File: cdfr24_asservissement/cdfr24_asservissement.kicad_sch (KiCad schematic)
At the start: 58 parts, among them J1 Connecteur batterie, J10 Free Connecteur, J11 Conn_01x02, J12 Conn_01x02, J13 Connecteur Odométrie, J2 Conn_01x03, J3 Conn_01x05, J4 Connecteur Programmation, J5 Conn_01x03, J6 Connecteur Odométrie, J7 Conn_01x03, Q13 Q_NMOS_GDS, U1 LM317_SOT-223, U3 STM32F401RCTx, U4 LMR16020PDDA, U4 LSM6DSL, Y1 Crystal_GND24

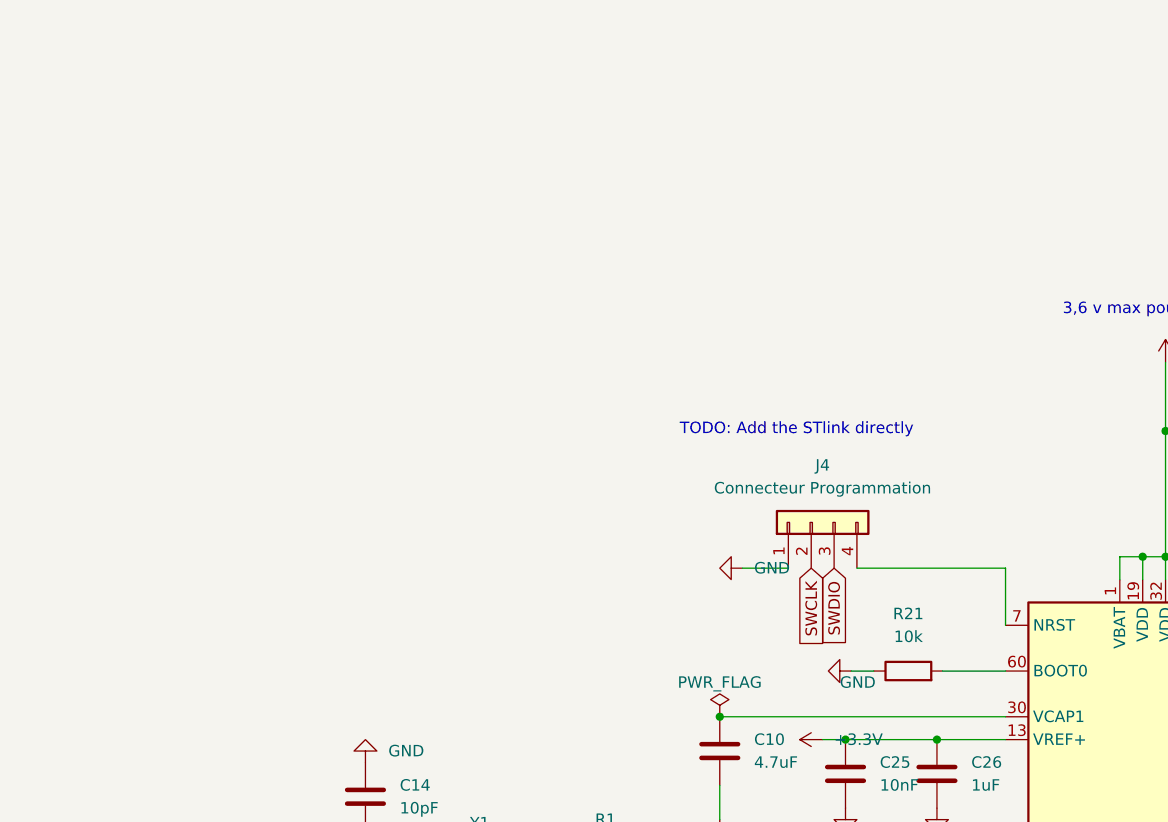
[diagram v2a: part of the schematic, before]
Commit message: new connecteur stlink
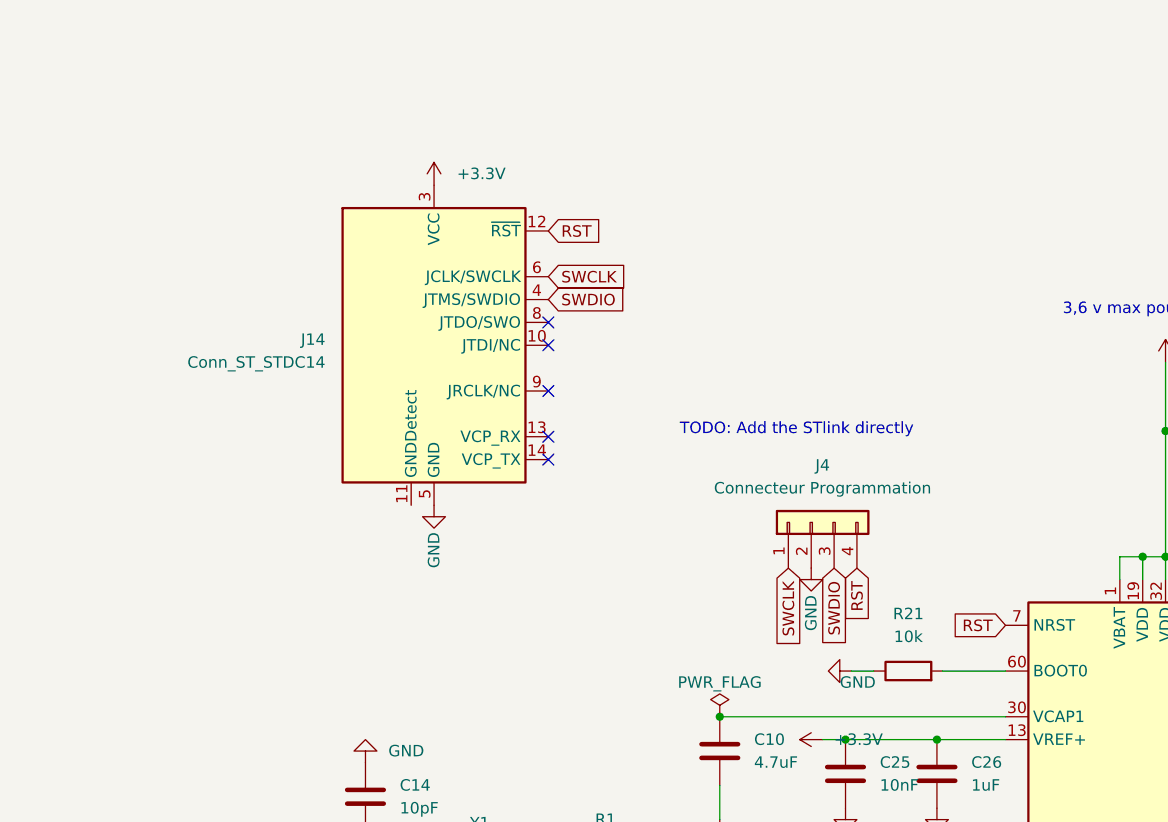
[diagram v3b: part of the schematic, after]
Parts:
- added J14: Conn_ST_STDC14, FTSH-107-01-L-DV-K-A:SAMTEC_FTSH-107-01-L-DV-K-A, symbol Connector:Conn_ST_STDC14
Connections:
- net +3.3V: now also J14.3 (VCC)
- net GND: now also J4.2 (Pin_2), J14.5 (GND), J14.7 (GND); no longer J4.1 (Pin_1)
- net SWCLK: now also J4.1 (Pin_1), J14.6 (JCLK/SWCLK); no longer J4.2 (Pin_2)
- net SWDIO: now also J14.4 (JTMS/SWDIO)
- net RST: now reaches J4.4 (Pin_4), U3.7 (NRST)
- net RST: now also J14.12 (~{RST})
- no-connect marks 15 -> 20
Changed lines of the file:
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@@
   (junction (at 145.415 236.22) (diameter 0) (color 0 0 0 0)
   )
+  (no_connect (at 79.375 225.425))
+  (no_connect (at 79.375 212.725))
   (no_connect (at 163.195 320.04))
   (no_connect (at 130.175 307.34))
@@
   (no_connect (at 163.195 289.56))
   (no_connect (at 130.175 309.88))
+  (no_connect (at 79.375 210.185))
   (no_connect (at 83.185 53.975))
   (no_connect (at 163.195 314.96))
@@
   (no_connect (at 163.195 269.24))
   (no_connect (at 130.175 279.4))
+  (no_connect (at 79.375 222.885))
   (no_connect (at 163.195 254))
+  (no_connect (at 79.375 217.805))
   (no_connect (at 163.195 264.16))
   (no_connect (at 163.195 307.34))
@@
     (stroke (width 0) (type default))
   )
-  (wire (pts (xy 113.665 237.49) (xy 130.175 237.49))
-    (stroke (width 0) (type default))
-  )
   (wire (pts (xy 145.415 236.22) (xy 147.955 236.22))
     (stroke (width 0) (type default))
@@
     (stroke (width 0) (type default))
   )
-  (wire (pts (xy 100.965 237.49) (xy 106.045 237.49))
-    (stroke (width 0) (type default))
-  )
   (wire (pts (xy 36.195 40.005) (xy 36.195 59.055))
     (stroke (width 0) (type default))
@@
     (stroke (width 0) (type default))
   )
-  (wire (pts (xy 130.175 237.49) (xy 130.175 243.84))
-    (stroke (width 0) (type default))
-  )
   (wire (pts (xy 222.885 280.67) (xy 229.235 280.67))
     (stroke (width 0) (type default))
@@
     )
   )
+  (global_label "SWDIO" (shape input) (at 79.375 207.645 0) (fields_autoplaced)
+    (effects (font (size 1.27 1.27)) (justify left))
+    (property "Intersheetrefs" "${INTERSHEET_REFS}" (at 88.147 207.645 0)
+      (effects (font (size 1.27 1.27)) (justify left) hide)
+    )
+  )
   (global_label "Free5" (shape input) (at 103.505 288.29 0) (fields_autoplaced)
     (effects (font (size 1.27 1.27)) (justify left))
@@
     )
   )
+  (global_label "RST" (shape input) (at 113.665 237.49 270) (fields_autoplaced)
+    (effects (font (size 1.27 1.27)) (justify right))
+    (property "Intersheetrefs" "${INTERSHEET_REFS}" (at 113.665 243.8429 90)
+      (effects (font (size 1.27 1.27)) (justify right) hide)
+    )
+  )
   (global_label "SWCLK" (shape input) (at 163.195 279.4 0) (fields_autoplaced)
     (effects (font (size 1.27 1.27)) (justify left))
@@
     )
   )
+  (global_label "SWCLK" (shape input) (at 79.375 205.105 0) (fields_autoplaced)
+    (effects (font (size 1.27 1.27)) (justify left))
+    (property "Intersheetrefs" "${INTERSHEET_REFS}" (at 88.5098 205.105 0)
+      (effects (font (size 1.27 1.27)) (justify left) hide)
+    )
+  )
   (global_label "Free6" (shape input) (at 103.505 290.83 0) (fields_autoplaced)
     (effects (font (size 1.27 1.27)) (justify left))
@@
     )
   )
+  (global_label "RST" (shape input) (at 79.375 200.025 0) (fields_autoplaced)
+    (effects (font (size 1.27 1.27)) (justify left))
+    (property "Intersheetrefs" "${INTERSHEET_REFS}" (at 85.7279 200.025 0)
+      (effects (font (size 1.27 1.27)) (justify left) hide)
+    )
+  )
   (global_label "Free7" (shape input) (at 103.505 293.37 0) (fields_autoplaced)
     (effects (font (size 1.27 1.27)) (justify left))
@@
     )
   )
-  (global_label "SWCLK" (shape input) (at 108.585 237.49 270) (fields_autoplaced)
+  (global_label "SWCLK" (shape input) (at 106.045 237.49 270) (fields_autoplaced)
     (effects (font (size 1.27 1.27)) (justify right))
-    (property "Intersheetrefs" "${INTERSHEET_REFS}" (at 108.6644 246.1321 90)
+    (property "Intersheetrefs" "${INTERSHEET_REFS}" (at 106.1244 246.1321 90)
       (effects (font (size 1.27 1.27)) (justify right) hide)
     )
@@
     )
   )
+  (global_label "RST" (shape input) (at 130.175 243.84 180) (fields_autoplaced)
+    (effects (font (size 1.27 1.27)) (justify right))
+    (property "Intersheetrefs" "${INTERSHEET_REFS}" (at 123.8221 243.84 0)
+      (effects (font (size 1.27 1.27)) (justify right) hide)
+    )
+  )
   (symbol (lib_id "power:+3.3V") (at 147.955 214.63 0) (unit 1)
     (in_bom yes) (on_board yes) (dnp no) (fields_autoplaced)
@@
     )
   )
-  (symbol (lib_id "power:GND") (at 100.965 237.49 270) (unit 1)
-    (in_bom yes) (on_board yes) (dnp no) (fields_autoplaced)
-    (property "Reference" "#PWR026" (at 94.615 237.49 0)
+  (symbol (lib_id "power:GND") (at 108.585 237.49 0) (unit 1)
+    (in_bom yes) (on_board yes) (dnp no)
+    (property "Reference" "#PWR026" (at 108.585 243.84 0)
       (effects (font (size 1.27 1.27)) hide)
     )
-    (property "Value" "GND" (at 102.235 237.4899 90)
+    (property "Value" "GND" (at 108.585 244.475 90)
       (effects (font (size 1.27 1.27)) (justify left))
     )
-    (property "Footprint" "" (at 100.965 237.49 0)
+    (property "Footprint" "" (at 108.585 237.49 0)
       (effects (font (size 1.27 1.27)) hide)
     )
-    (property "Datasheet" "" (at 100.965 237.49 0)
+    (property "Datasheet" "" (at 108.585 237.49 0)
       (effects (font (size 1.27 1.27)) hide)
     )
@@
     )
   )
+  (symbol (lib_id "power:+3.3V") (at 66.675 194.945 0) (unit 1)
+    (in_bom yes) (on_board yes) (dnp no) (fields_autoplaced)
+    (property "Reference" "#PWR025" (at 66.675 198.755 0)
+      (effects (font (size 1.27 1.27)) hide)
+    )
+    (property "Value" "+3.3V" (at 69.215 193.6749 0)
+      (effects (font (size 1.27 1.27)) (justify left))
+    )
+    (property "Footprint" "" (at 66.675 194.945 0)
+      (effects (font (size 1.27 1.27)) hide)
+    )
+    (property "Datasheet" "" (at 66.675 194.945 0)
+      (effects (font (size 1.27 1.27)) hide)
+    )
+    (pin "1")
+    (instances
+      (project "Asservissement_CDFR_2023"
+        (path "/aba37299-4f54-471d-ab35-d760532fd54c"
+          (reference "#PWR025") (unit 1)
+        )
+      )
+      (project "cdfr24_asservissement"
+        (path "/c6b82269-16f5-49e6-8b51-4d12a40a3077"
+          (reference "#PWR043") (unit 1)
+        )
+      )
+    )
+  )
   (symbol (lib_id "Device:Crystal_GND24") (at 59.055 270.51 90) (unit 1)
     (in_bom yes) (on_board yes) (dnp no) (fields_autoplaced)
@@
     )
   )
+  (symbol (lib_id "Connector:Conn_ST_STDC14") (at 66.675 212.725 0) (unit 1)
+    (in_bom yes) (on_board yes) (dnp no) (fields_autoplaced)
+    (property "Reference" "J14" (at 54.61 212.09 0)
+      (effects (font (size 1.27 1.27)) (justify right))
+    )
+    (property "Value" "Conn_ST_STDC14" (at 54.61 214.63 0)
+      (effects (font (size 1.27 1.27)) (justify right))
+    )
+    (property "Footprint" "FTSH-107-01-L-DV-K-A:SAMTEC_FTSH-107-01-L-DV-K-A" (at 66.675 212.725 0)
+      (effects (font (size 1.27 1.27)) hide)
+    )
+    (property "Datasheet" "https://www.st.com/content/ccc/resource/technical/document/user_manual/group1/99/49/91/b6/b2/3a/46/e5/DM00526767/files/DM00526767.pdf/jcr:content/translations/en.DM00526767.pdf" (at 57.785 244.475 90)
+      (effects (font (size 1.27 1.27)) hide)
+    )
+    (pin "1")
+    (pin "10")
+    (pin "11")
+    (pin "12")
+    (pin "13")
+    (pin "14")
+    (pin "2")
+    (pin "3")
+    (pin "4")
+    (pin "5")
+    (pin "6")
+    (pin "7")
+    (pin "8")
+    (pin "9")
+    (instances
+      (project "cdfr24_asservissement"
+        (path "/c6b82269-16f5-49e6-8b51-4d12a40a3077"
+          (reference "J14") (unit 1)
+        )
+      )
+    )
+  )
   (symbol (lib_id "Connector_Generic:Conn_01x02") (at 71.755 331.47 90) (mirror x) (unit 1)
     (in_bom yes) (on_board yes) (dnp no) (fields_autoplaced)
@@
         )
       )
+    )
+  )
+  (symbol (lib_id "power:GND") (at 66.675 230.505 0) (unit 1)
+    (in_bom yes) (on_board yes) (dnp no)
+    (property "Reference" "#PWR026" (at 66.675 236.855 0)
+      (effects (font (size 1.27 1.27)) hide)
+    )
+    (property "Value" "GND" (at 66.675 237.49 90)
+      (effects (font (size 1.27 1.27)) (justify left))
+    )
+    (property "Footprint" "" (at 66.675 230.505 0)
+      (effects (font (size 1.27 1.27)) hide)
+    )
+    (property "Datasheet" "" (at 66.675 230.505 0)
+      (effects (font (size 1.27 1.27)) hide)
+    )
+    (pin "1")
+    (instances
+      (project "Asservissement_CDFR_2023"
+        (path "/aba37299-4f54-471d-ab35-d760532fd54c"
+          (reference "#PWR026") (unit 1)
+        )
+      )
+      (project "cdfr24_asservissement"
+        (path "/c6b82269-16f5-49e6-8b51-4d12a40a3077"
+          (reference "#PWR015") (unit 1)
+        )
+      )
